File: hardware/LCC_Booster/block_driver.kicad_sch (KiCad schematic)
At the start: 19 parts, among them Q1 AO3400A, U10 7410, U6 DRV8874PWPR, U7 7410, U8 7410, U9 7410

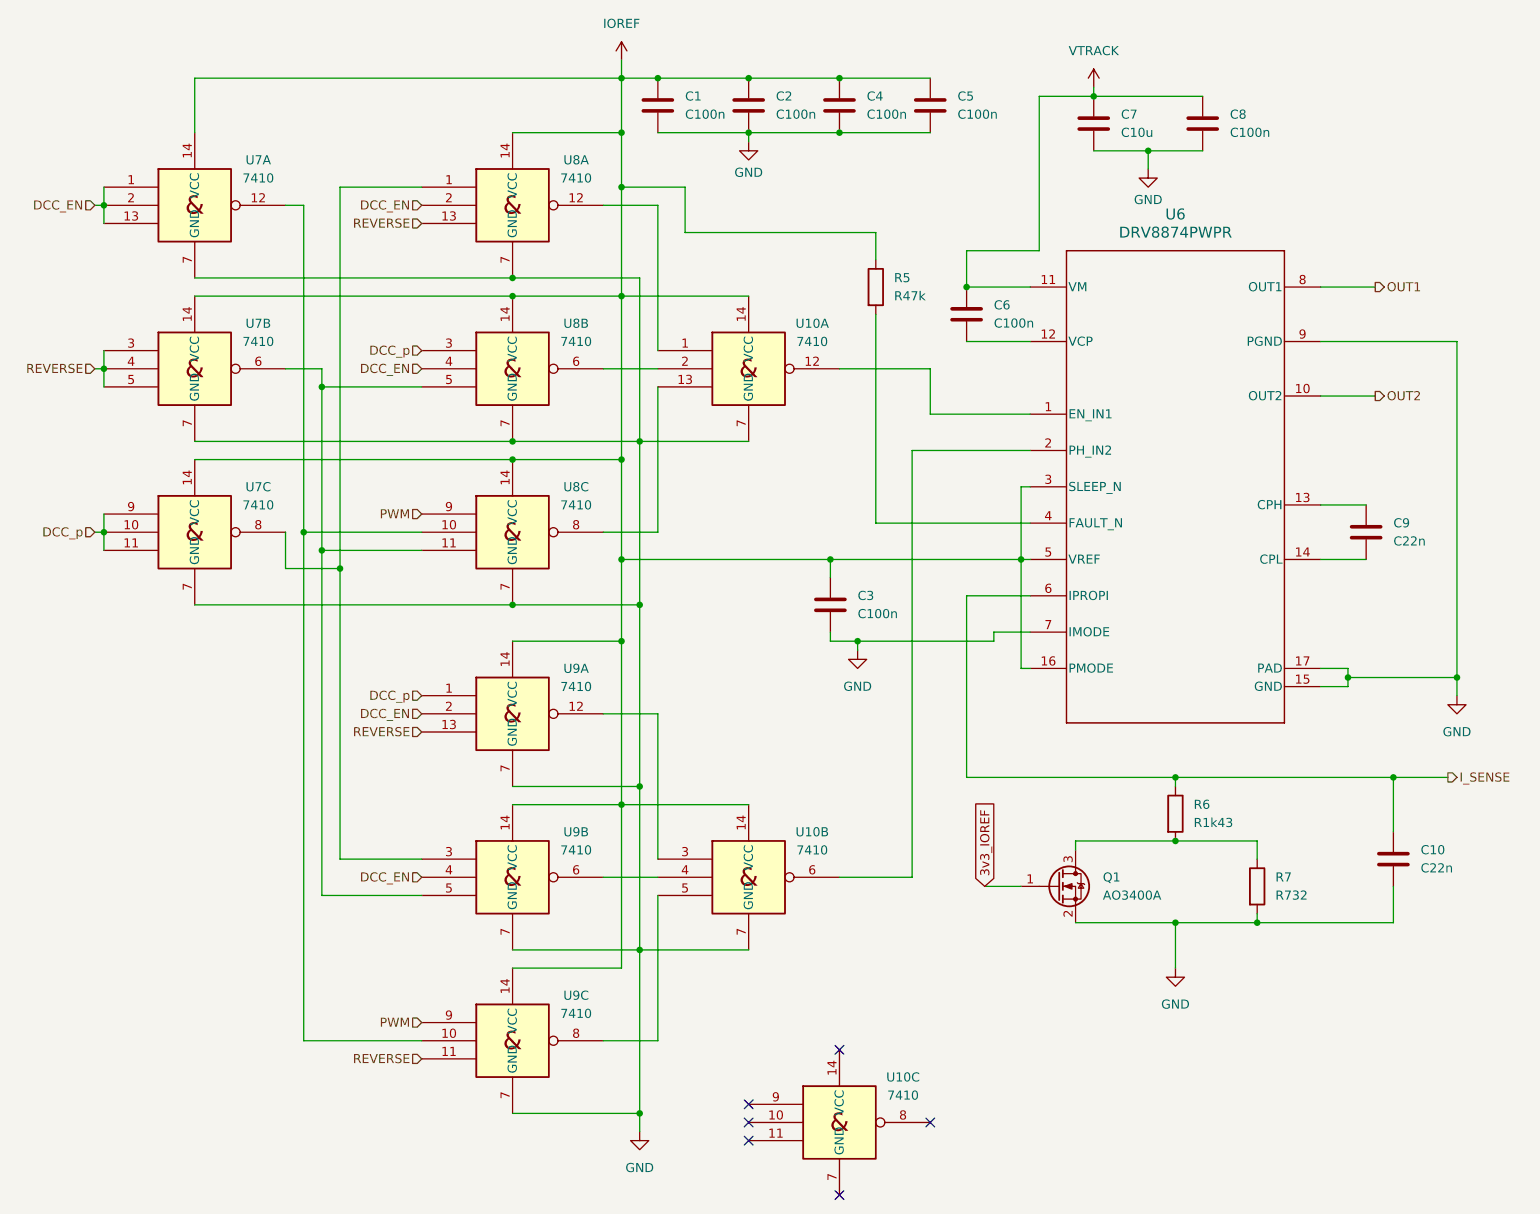
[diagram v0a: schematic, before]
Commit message: Switch to single Arduino per board
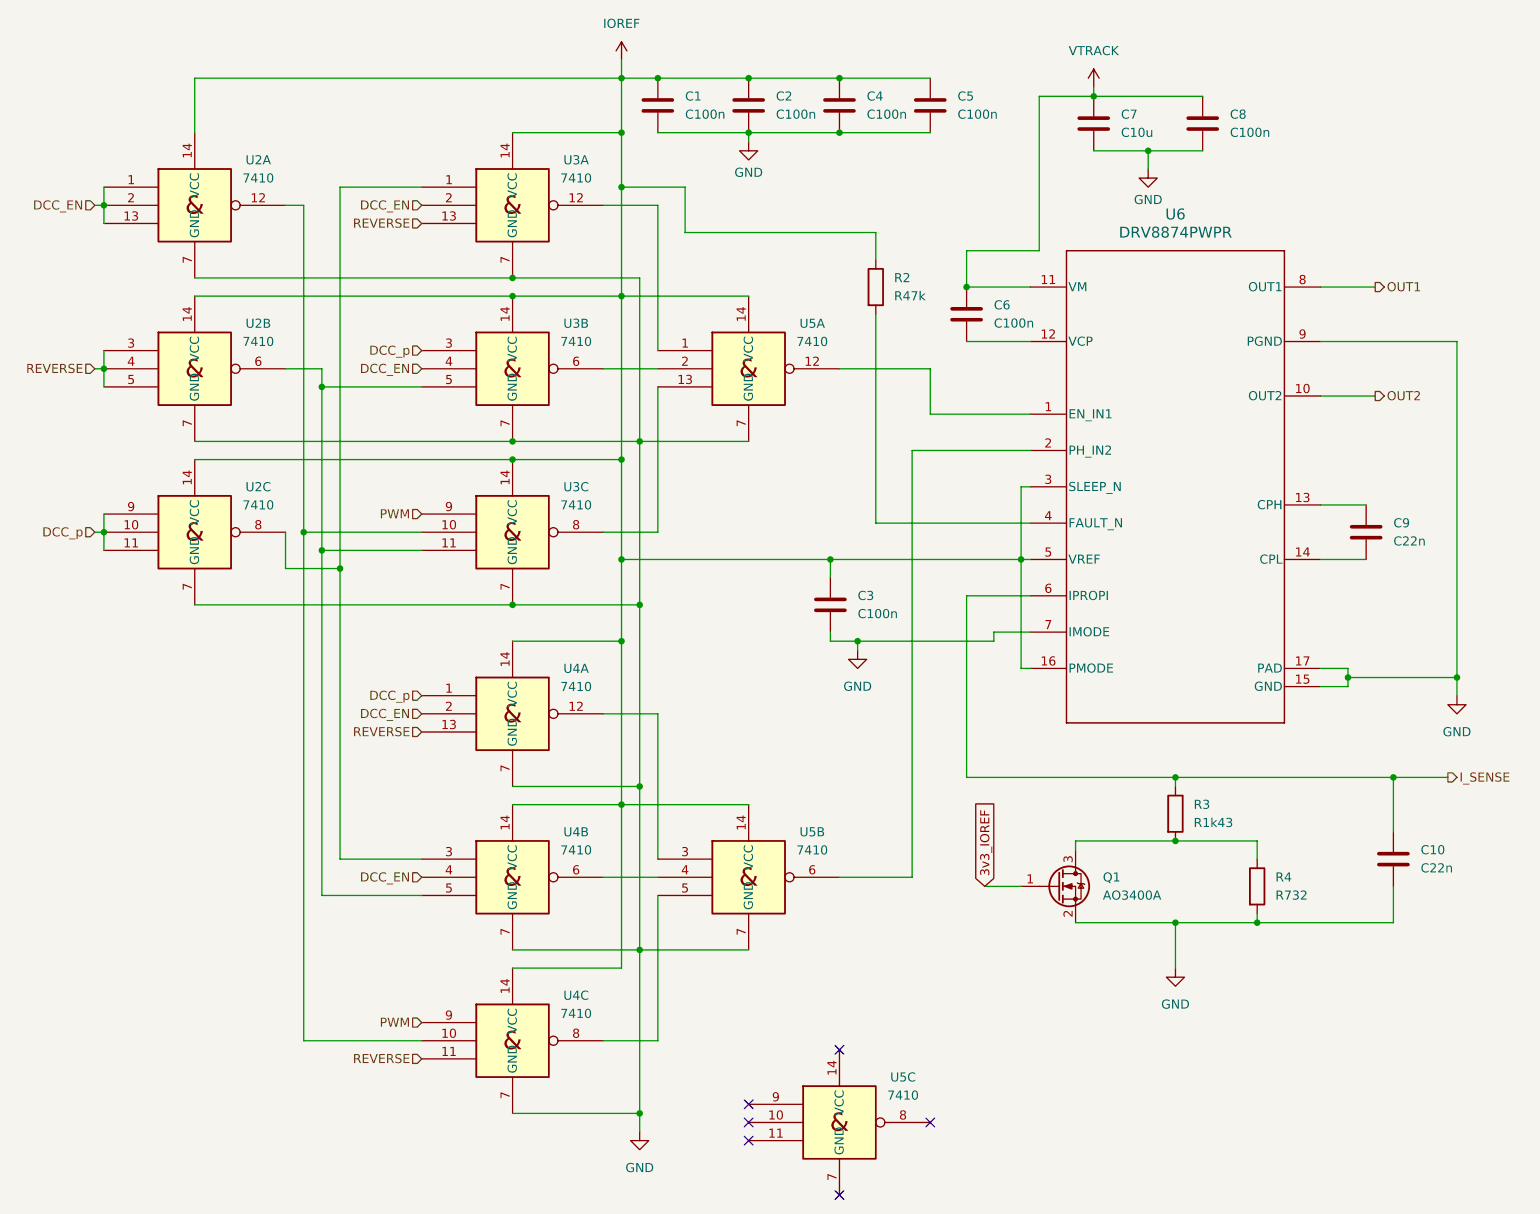
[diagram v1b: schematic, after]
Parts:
- C1, C10, C2, C3, C4, C5, C6, C8, C9: footprint Capacitor_SMD:C_1206_3216Metric_Pad1.33x1.80mm_HandSolder -> Capacitor_SMD:C_0402_1005Metric_Pad0.74x0.62mm_HandSolder
- U6: footprint footprints:PWP0016J_NV -> DRV8874:PWP0016J_NV
- renumbered R5 to R2, R6 to R3, R7 to R4, U7 to U2, U8 to U3, U9 to U4, U10 to U5

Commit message: Small Tweaks
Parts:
- R1: renamed from R2; footprint Resistor_SMD:R_0815_2038Metric_Pad1.20x4.05mm_HandSolder -> Resistor_SMD:R_01005_0402Metric_Pad0.57x0.30mm_HandSolder
- R2: renamed from R3; footprint Resistor_SMD:R_0815_2038Metric_Pad1.20x4.05mm_HandSolder -> Resistor_SMD:R_01005_0402Metric_Pad0.57x0.30mm_HandSolder
- R3: renamed from R4; footprint Resistor_SMD:R_0815_2038Metric_Pad1.20x4.05mm_HandSolder -> Resistor_SMD:R_01005_0402Metric_Pad0.57x0.30mm_HandSolder
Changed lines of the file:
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@@
 		(dnp no)
 		(fields_autoplaced yes)
-		(property "Reference" "R3"
+		(property "Reference" "R2"
 			(at 203.2 130.8099 0)
 			(effects
@@
 			)
 		)
-		(property "Footprint" "Resistor_SMD:R_0815_2038Metric_Pad1.20x4.05mm_HandSolder"
+		(property "Footprint" "Resistor_SMD:R_01005_0402Metric_Pad0.57x0.30mm_HandSolder"
 			(at 198.882 132.08 90)
 			(effects
@@
 			(project "LCC_Booster"
 				(path "/e8524381-bb01-4107-93ec-8133e878a3da/e60b84bd-96a5-4d6c-8d17-0e1e474b63f1"
-					(reference "R3")
+					(reference "R2")
 					(unit 1)
 				)
 				(path "/e8524381-bb01-4107-93ec-8133e878a3da/d1a66b1c-451f-4d75-a19b-2f867b2d97ed"
-					(reference "R6")
+					(reference "R5")
 					(unit 1)
 				)
 				(path "/e8524381-bb01-4107-93ec-8133e878a3da/3acc3266-052e-42c0-b497-1dc12936230d"
-					(reference "R9")
+					(reference "R8")
 					(unit 1)
 				)
 				(path "/e8524381-bb01-4107-93ec-8133e878a3da/6939f6fa-d75b-4eb8-b744-4876a3adabd6"
-					(reference "R12")
+					(reference "R11")
 					(unit 1)
 				)
@@
 		(dnp no)
 		(fields_autoplaced yes)
-		(property "Reference" "R2"
+		(property "Reference" "R1"
 			(at 161.29 57.1499 0)
 			(effects
@@
 			)
 		)
-		(property "Footprint" "Resistor_SMD:R_0815_2038Metric_Pad1.20x4.05mm_HandSolder"
+		(property "Footprint" "Resistor_SMD:R_01005_0402Metric_Pad0.57x0.30mm_HandSolder"
 			(at 156.972 58.42 90)
 			(effects
@@
 			(project "LCC_Booster"
 				(path "/e8524381-bb01-4107-93ec-8133e878a3da/e60b84bd-96a5-4d6c-8d17-0e1e474b63f1"
-					(reference "R2")
+					(reference "R1")
 					(unit 1)
 				)
 				(path "/e8524381-bb01-4107-93ec-8133e878a3da/d1a66b1c-451f-4d75-a19b-2f867b2d97ed"
-					(reference "R5")
+					(reference "R4")
 					(unit 1)
 				)
 				(path "/e8524381-bb01-4107-93ec-8133e878a3da/3acc3266-052e-42c0-b497-1dc12936230d"
-					(reference "R8")
+					(reference "R7")
 					(unit 1)
 				)
 				(path "/e8524381-bb01-4107-93ec-8133e878a3da/6939f6fa-d75b-4eb8-b744-4876a3adabd6"
-					(reference "R11")
+					(reference "R10")
 					(unit 1)
 				)
@@
 		(dnp no)
 		(fields_autoplaced yes)
-		(property "Reference" "R4"
+		(property "Reference" "R3"
 			(at 214.63 140.9699 0)
 			(effects
@@
 			)
 		)
-		(property "Footprint" "Resistor_SMD:R_0815_2038Metric_Pad1.20x4.05mm_HandSolder"
+		(property "Footprint" "Resistor_SMD:R_01005_0402Metric_Pad0.57x0.30mm_HandSolder"
 			(at 210.312 142.24 90)
 			(effects
@@
 			(project "LCC_Booster"
 				(path "/e8524381-bb01-4107-93ec-8133e878a3da/e60b84bd-96a5-4d6c-8d17-0e1e474b63f1"
-					(reference "R4")
+					(reference "R3")
 					(unit 1)
 				)
 				(path "/e8524381-bb01-4107-93ec-8133e878a3da/d1a66b1c-451f-4d75-a19b-2f867b2d97ed"
-					(reference "R7")
+					(reference "R6")
 					(unit 1)
 				)
 				(path "/e8524381-bb01-4107-93ec-8133e878a3da/3acc3266-052e-42c0-b497-1dc12936230d"
-					(reference "R10")
+					(reference "R9")
 					(unit 1)
 				)
 				(path "/e8524381-bb01-4107-93ec-8133e878a3da/6939f6fa-d75b-4eb8-b744-4876a3adabd6"
-					(reference "R13")
+					(reference "R12")
 					(unit 1)
 				)

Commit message: LCC Command Station Shield
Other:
- company: (none) -> TMRC
- title: (none) -> Arduino Nano LCC Booster
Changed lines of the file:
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@@
 	(generator_version "8.0")
 	(paper "A4")
+	(title_block
+		(title "Arduino Nano LCC Booster")
+		(date "2024-04-28")
+		(rev "1.0")
+		(company "TMRC")
+		(comment 1 "Noah Paladino")
+	)
 	(junction
 		(at 196.85 39.37)

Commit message: Update to hardware v2 and cleanup
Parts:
- removed C1, C4, C5: C100n, Capacitor_SMD:C_0402_1005Metric_Pad0.74x0.62mm_HandSolder, symbol Device:C
- removed Q1: AO3400A, Package_TO_SOT_SMD:SOT-23, symbol Transistor_FET:AO3400A
- removed U2, U3, U4, U5: 7410, Package_SO:SOIC-14_3.9x8.7mm_P1.27mm, symbol 74xx_IEEE:7410
- added JP4: SolderJumper_2_Bridged, Jumper:SolderJumper-2_P1.3mm_Bridged_RoundedPad1.0x1.5mm, symbol Jumper:SolderJumper_2_Bridged
- added U3: SN74HC253DR, Package_SO:SO-16_3.9x9.9mm_P1.27mm, symbol SN74HC253DR:SN74HC253DR
- R3: now not fitted
- renumbered C2 to C1, C3 to C2, C6 to C3, C7 to C4, C8 to C5, C9 to C6, C10 to C7, U6 to U4
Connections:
- net DCC_EN: now also U3.2 (B)
- net DCC_p: now also U3.13 (2C3), U3.4 (1C2)
- net GND: now also JP4.1 (A), U3.1 (*1OE), U3.10 (2C0), U3.15 (*2OE), U3.5 (1C1), U3.8 (GND)
- net IOREF: now also U3.16 (VCC)
- net PWM: now also U3.11 (2C1), U3.6 (1C0)
- net REVERSE: now also U3.14 (A)
- net at R2.2, R3.1: now also JP4.2 (B)
- net at U4.2 (PH_IN2): now also U3.9 (2Y)
- net at U4.1 (EN_IN1): now also U3.7 (1Y)
- new net DCC_n: U3.12 (2C2), U3.3 (1C3)
- no-connect marks 6 -> 0

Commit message: Update Schematic
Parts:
- renumbered C1 to C15, C2 to C16, C3 to C17, C4 to C18, C5 to C19, C6 to C20, C7 to C21, JP4 to JP6, R1 to R7, R2 to R8, R3 to R9, U3 to U7, U4 to U8

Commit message: Add Fault Pin Inputs to Arduino
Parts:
- JP6: value SolderJumper_2_Bridged -> SolderJumper_2; footprint Jumper:SolderJumper-2_P1.3mm_Bridged_RoundedPad1.0x1.5mm -> Jumper:SolderJumper-2_P1.3mm_Open_RoundedPad1.0x1.5mm; symbol Jumper:SolderJumper_2_Bridged -> Jumper:SolderJumper_2_Open
- R8: value R1k43 -> R1k430
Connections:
- net nFAULT: now reaches R7.2, U8.4 (FAULT_N)
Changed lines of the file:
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@@
 	(title_block
 		(title "Arduino Nano LCC Booster")
-		(date "2024-05-14")
-		(rev "2")
+		(date "2024-09-10")
+		(rev "4")
 		(company "TMRC")
 		(comment 1 "Noah Paladino")
@@
 	)
 	(junction
+		(at 158.75 91.44)
+		(diameter 0)
+		(color 0 0 0 0)
+	)
+	(junction
 		(at 54.61 78.74)
 		(diameter 0)
@@
 		(pts
 			(xy 130.81 76.2) (xy 130.81 87.63)
+		)
+		(stroke
+			(width 0)
+			(type default)
+		)
+	)
+	(wire
+		(pts
+			(xy 142.24 91.44) (xy 158.75 91.44)
 		)
 		(stroke
@@
 		)
 	)
+	(hierarchical_label "nFAULT"
+		(shape output)
+		(at 142.24 91.44 180)
+		(fields_autoplaced yes)
+		(effects
+			(font
+				(size 1.27 1.27)
+			)
+			(justify right)
+		)
+	)
 	(hierarchical_label "OUT2"
 		(shape output)
@@
 	)
 	(symbol
-		(lib_id "Jumper:SolderJumper_2_Bridged")
+		(lib_id "Jumper:SolderJumper_2_Open")
 		(at 186.69 142.24 90)
 		(unit 1)
@@
 			)
 		)
-		(property "Value" "SolderJumper_2_Bridged"
+		(property "Value" "SolderJumper_2"
 			(at 189.23 143.5099 90)
 			(effects
@@
 			)
 		)
-		(property "Footprint" "Jumper:SolderJumper-2_P1.3mm_Bridged_RoundedPad1.0x1.5mm"
+		(property "Footprint" "Jumper:SolderJumper-2_P1.3mm_Open_RoundedPad1.0x1.5mm"
 			(at 186.69 142.24 0)
 			(effects
@@
 			)
 		)
-		(property "Description" "Solder Jumper, 2-pole, closed/bridged"
+		(property "Description" "Solder Jumper, 2-pole, open"
 			(at 186.69 142.24 0)
 			(effects
@@
 			)
 		)
-		(property "Value" "R1k43"
+		(property "Value" "R1k430"
 			(at 203.2 133.3499 0)
 			(effects

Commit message: Update for PCB Assembly
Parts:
- C15, C16, C17: MANUFACTURER (none) -> Samsung; Manufacturer Part Number (none) -> CL05B104K05NNNC
- C18: value C10u -> C10u VM; MANUFACTURER (none) -> Samsung; Manufacturer Part Number (none) -> CL31A106KBHNNNE
- C19: value C100n -> C100n VM; MANUFACTURER (none) -> Samsung; Manufacturer Part Number (none) -> CL05B104KB5NFNC
- C20, C21: MANUFACTURER (none) -> Samsung; Manufacturer Part Number (none) -> CL05B223KB5NNNC
- R7: footprint Resistor_SMD:R_01005_0402Metric_Pad0.57x0.30mm_HandSolder -> Resistor_SMD:R_0805_2012Metric_Pad1.20x1.40mm_HandSolder; MANUFACTURER (none) -> Panasonic; Manufacturer Part Number (none) -> ERJ6ENF4702V
- R8: footprint Resistor_SMD:R_01005_0402Metric_Pad0.57x0.30mm_HandSolder -> Resistor_SMD:R_0402_1005Metric_Pad0.72x0.64mm_HandSolder; MANUFACTURER (none) -> Yageo; Manufacturer Part Number (none) -> AC0402FR-071K43L
- R9: footprint Resistor_SMD:R_01005_0402Metric_Pad0.57x0.30mm_HandSolder -> Resistor_SMD:R_0402_1005Metric_Pad0.72x0.64mm_HandSolder
- U5: renamed from U7; MANUFACTURER (none) -> TI; Manufacturer Part Number (none) -> SN74HC253DR
- U6: renamed from U8; MANUFACTURER (none) -> TI; Manufacturer Part Number (none) -> DRV8874PWPR
- renumbered JP6 to JP8
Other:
- moved on the sheet: C19
